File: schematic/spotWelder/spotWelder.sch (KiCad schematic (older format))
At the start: 18 parts, among them J1 InterBoard, Q1 Q_NPN_BCE, SW1 Rotary_Encoder_Switch, U1 STM32F103CBTx, U2 SSD1306-I2C-OLED-128x64, U3 DC/DC converter

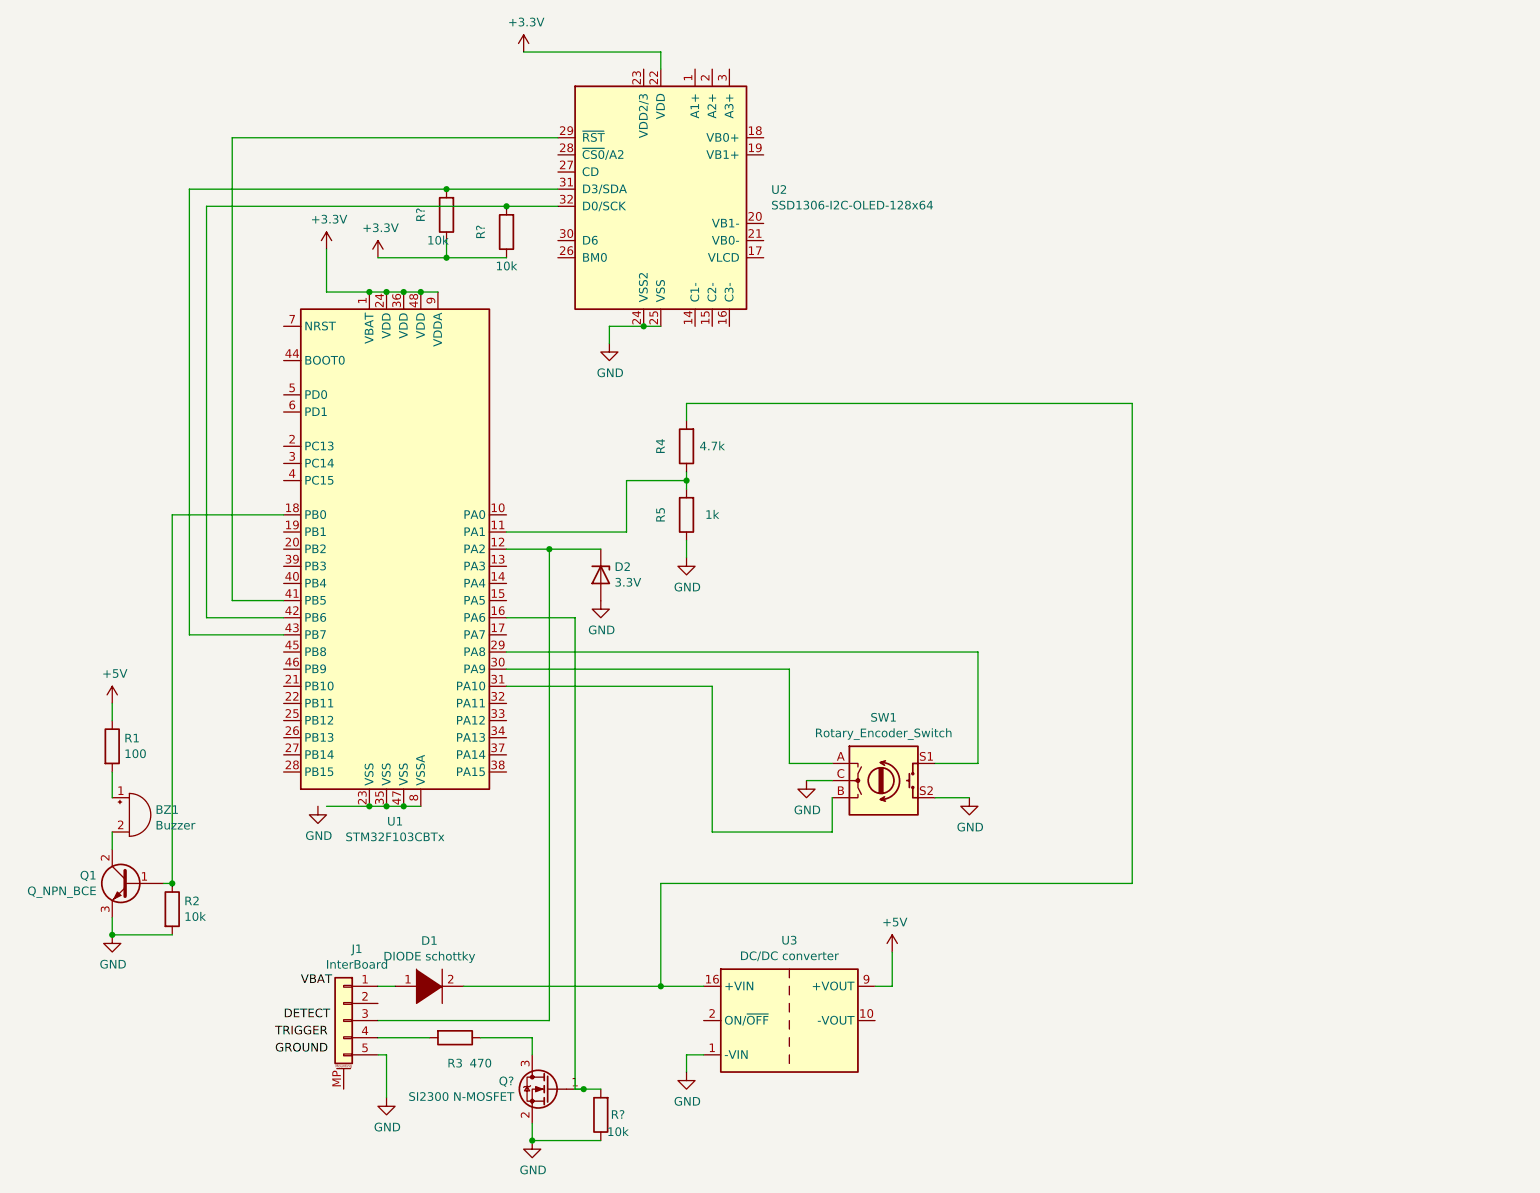
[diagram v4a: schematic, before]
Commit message: add pedal to schematic
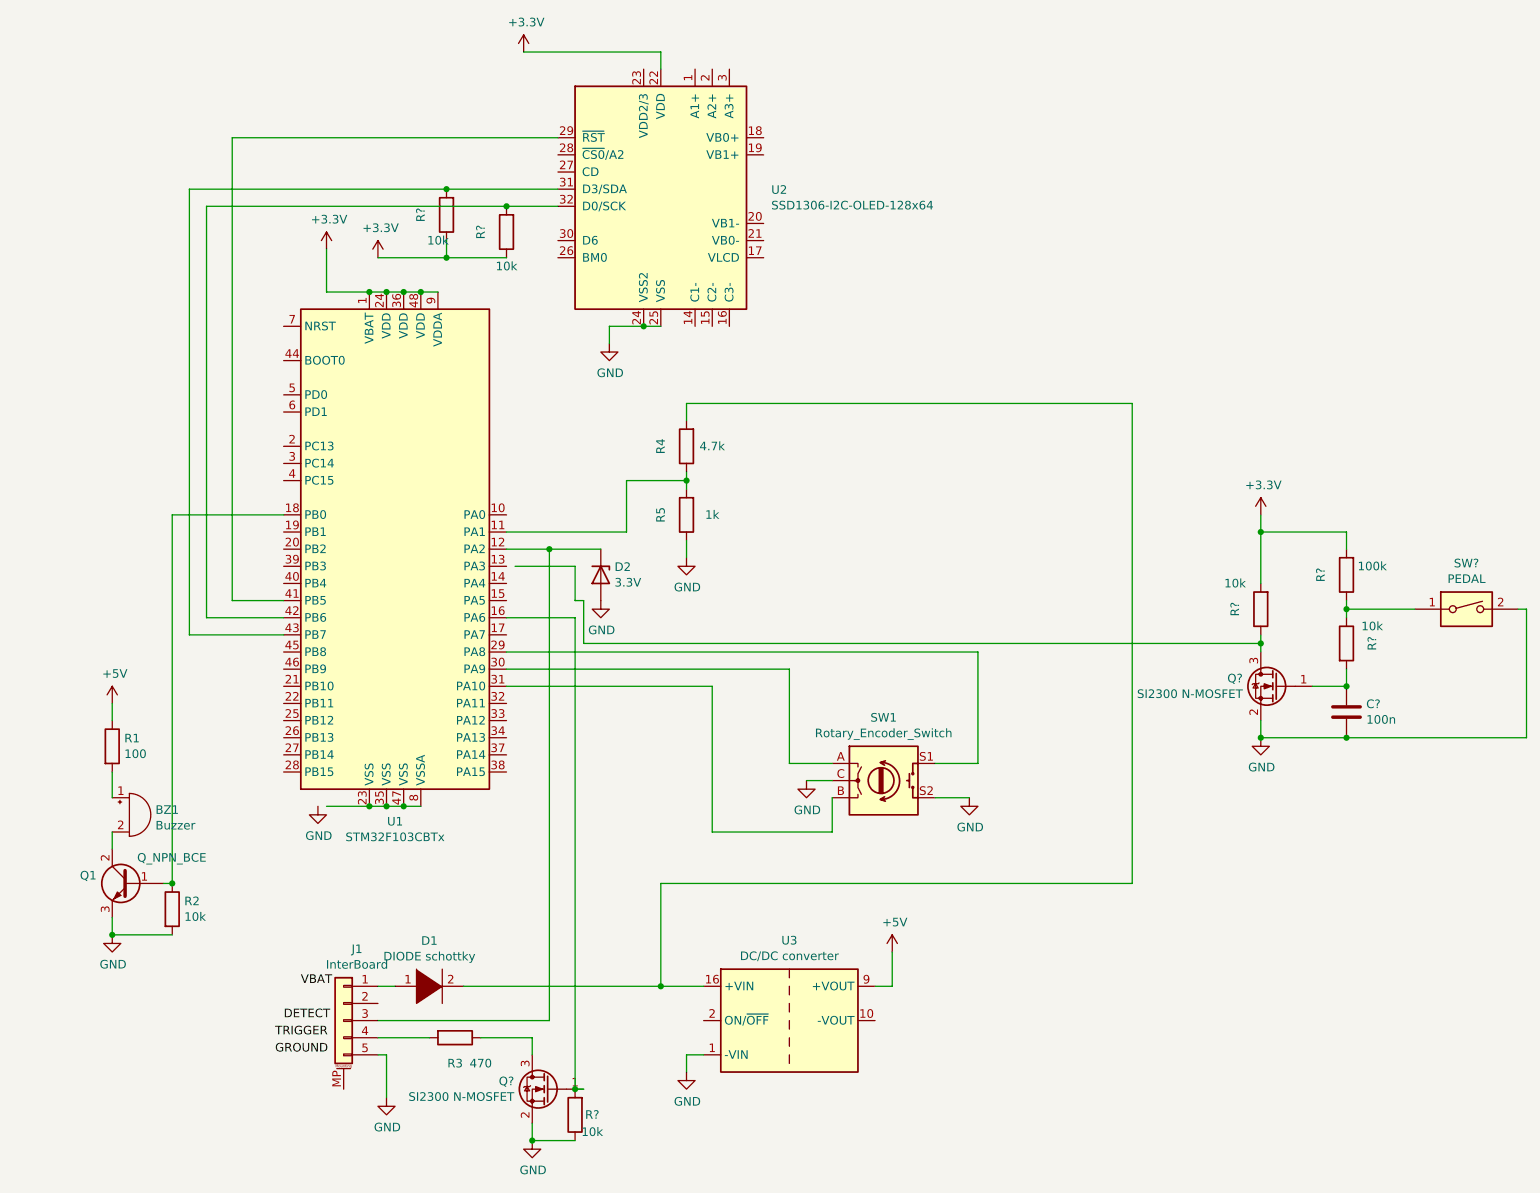
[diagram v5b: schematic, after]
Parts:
- added C?: 100n, symbol Device:C
- added Q?: SI2300 N-MOSFET, Package_TO_SOT_SMD:SOT-23, symbol Transistor_FET:ZXMN2A01F
- added R? (x2): 10k, symbol Device:R
- added R?: 100k, symbol Device:R
- added SW?: PEDAL, symbol Switch:SW_DIP_x01
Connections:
- net +3V3: now also R?.2, R?.2
- net GND: now also C?.2, Q?.2 (S), SW?.2
- new net: C?.1, Q?.1 (G), R?.2
- new net: Q?.3 (D), R?.1
- new net: R?.1, R?.1, SW?.1
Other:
- moved on the sheet: R?
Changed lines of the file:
@@
 P 900 5550
 F 0 "Q1" H 1091 5596 50  0000 L CNN
-F 1 "Q_NPN_BCE" H 1091 5505 50  0000 L CNN
+F 1 "Q_NPN_BCE" H 450 5700 50  0000 L CNN
 F 2 "" H 1100 5650 50  0001 C CNN
 F 3 "~" H 900 5550 50  0001 C CNN
@@
 L Device:R R?
 U 1 1 606079F6
-P 3650 6900
-F 0 "R?" H 3550 6900 50  0000 C CNN
-F 1 "10k" H 3550 7000 50  0000 C CNN
-F 2 "" V 3580 6900 50  0001 C CNN
-F 3 "~" H 3650 6900 50  0001 C CNN
-	1    3650 6900
-	-1   0    0    1
-$EndComp
-Wire Wire Line
-	3550 6750 3650 6750
-Wire Wire Line
-	3650 7050 3250 7050
+P 3500 6900
+F 0 "R?" H 3400 6900 50  0000 C CNN
+F 1 "10k" H 3400 7000 50  0000 C CNN
+F 2 "" V 3430 6900 50  0001 C CNN
+F 3 "~" H 3500 6900 50  0001 C CNN
+	1    3500 6900
+	-1   0    0    1
+$EndComp
 Connection ~ 3250 7050
 Wire Wire Line
 	3500 4000 3500 6750
-Wire Wire Line
-	3500 6750 3550 6750
-Connection ~ 3550 6750
+$Comp
+L Transistor_FET:ZXMN2A01F Q?
+U 1 1 6062FDB3
+P 7600 4400
+F 0 "Q?" H 7805 4446 50  0000 L CNN
+F 1 "SI2300 N-MOSFET" H 7805 4355 50  0000 L CNN
+F 2 "Package_TO_SOT_SMD:SOT-23" H 7800 4325 50  0001 L CIN
+F 3 "http://www.diodes.com/assets/Datasheets/ZXMN2A01F.pdf" H 7600 4400 50  0001 L CNN
+	1    7600 4400
+	-1   0    0    -1
+$EndComp
+$Comp
+L power:GND #PWR?
+U 1 1 606358E9
+P 7500 4700
+F 0 "#PWR?" H 7500 4450 50  0001 C CNN
+F 1 "GND" H 7505 4527 50  0000 C CNN
+F 2 "" H 7500 4700 50  0001 C CNN
+F 3 "" H 7500 4700 50  0001 C CNN
+	1    7500 4700
+	1    0    0    -1
+$EndComp
+$Comp
+L power:+3.3V #PWR?
+U 1 1 60637134
+P 7500 3400
+F 0 "#PWR?" H 7500 3250 50  0001 C CNN
+F 1 "+3.3V" H 7515 3573 50  0000 C CNN
+F 2 "" H 7500 3400 50  0001 C CNN
+F 3 "" H 7500 3400 50  0001 C CNN
+	1    7500 3400
+	1    0    0    -1
+$EndComp
+$Comp
+L Device:R R?
+U 1 1 60639461
+P 8000 4150
+F 0 "R?" V 8150 4150 50  0000 C CNN
+F 1 "10k" H 8150 4250 50  0000 C CNN
+F 2 "" V 7930 4150 50  0001 C CNN
+F 3 "~" H 8000 4150 50  0001 C CNN
+	1    8000 4150
+	1    0    0    -1
+$EndComp
+$Comp
+L Device:R R?
+U 1 1 6063CBA6
+P 8000 3750
+F 0 "R?" V 8150 3750 50  0000 C CNN
+F 1 "100k" H 7850 3700 50  0000 C CNN
+F 2 "" V 7930 3750 50  0001 C CNN
+F 3 "~" H 8000 3750 50  0001 C CNN
+	1    8000 3750
+	-1   0    0    1
+$EndComp
+$Comp
+L Device:R R?
+U 1 1 6063D28E
+P 7500 3950
+F 0 "R?" V 7650 3950 50  0000 C CNN
+F 1 "10k" H 7650 3800 50  0000 C CNN
+F 2 "" V 7430 3950 50  0001 C CNN
+F 3 "~" H 7500 3950 50  0001 C CNN
+	1    7500 3950
+	-1   0    0    1
+$EndComp
+Wire Wire Line
+	7500 4600 7500 4700
+Connection ~ 7500 4700
+Wire Wire Line
+	7500 4200 7500 4150
+Wire Wire Line
+	3150 3700 3500 3700
+Wire Wire Line
+	3500 3700 3500 3900
+Wire Wire Line
+	3500 3900 3550 3900
+Wire Wire Line
+	3550 3900 3550 4150
+Connection ~ 7500 4150
+Wire Wire Line
+	7500 4150 7500 4100
+$Comp
+L Device:C C?
+U 1 1 6065972F
+P 8000 4550
+F 0 "C?" H 8115 4596 50  0000 L CNN
+F 1 "100n" H 8115 4505 50  0000 L CNN
+F 2 "" H 8038 4400 50  0001 C CNN
+F 3 "~" H 8000 4550 50  0001 C CNN
+	1    8000 4550
+	1    0    0    -1
+$EndComp
+Wire Wire Line
+	7500 4700 8000 4700
+$Comp
+L Switch:SW_DIP_x01 SW?
+U 1 1 6066CEBA
+P 8700 3950
+F 0 "SW?" H 8700 4217 50  0000 C CNN
+F 1 "PEDAL" H 8700 4126 50  0000 C CNN
+F 2 "" H 8700 3950 50  0001 C CNN
+F 3 "~" H 8700 3950 50  0001 C CNN
+	1    8700 3950
+	1    0    0    -1
+$EndComp
+Wire Wire Line
+	7800 4400 8000 4400
+Connection ~ 8000 4700
+Wire Wire Line
+	8000 4700 9050 4700
+Wire Wire Line
+	7500 3400 7500 3500
+Wire Wire Line
+	7500 3500 8000 3500
+Wire Wire Line
+	8000 3500 8000 3600
+Connection ~ 7500 3500
+Wire Wire Line
+	7500 3500 7500 3800
+Wire Wire Line
+	8000 3900 8000 3950
+Wire Wire Line
+	8000 4300 8000 4400
+Connection ~ 8000 4400
+Wire Wire Line
+	9000 3950 9050 3950
+Wire Wire Line
+	9050 3950 9050 4700
+Wire Wire Line
+	8400 3950 8000 3950
+Connection ~ 8000 3950
+Wire Wire Line
+	8000 3950 8000 4000
+Wire Wire Line
+	3500 7050 3250 7050
+Wire Wire Line
+	3550 6750 3500 6750
+Connection ~ 3500 6750
+Wire Wire Line
+	3550 4150 7500 4150
 $EndSCHEMATC

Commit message: update schematic
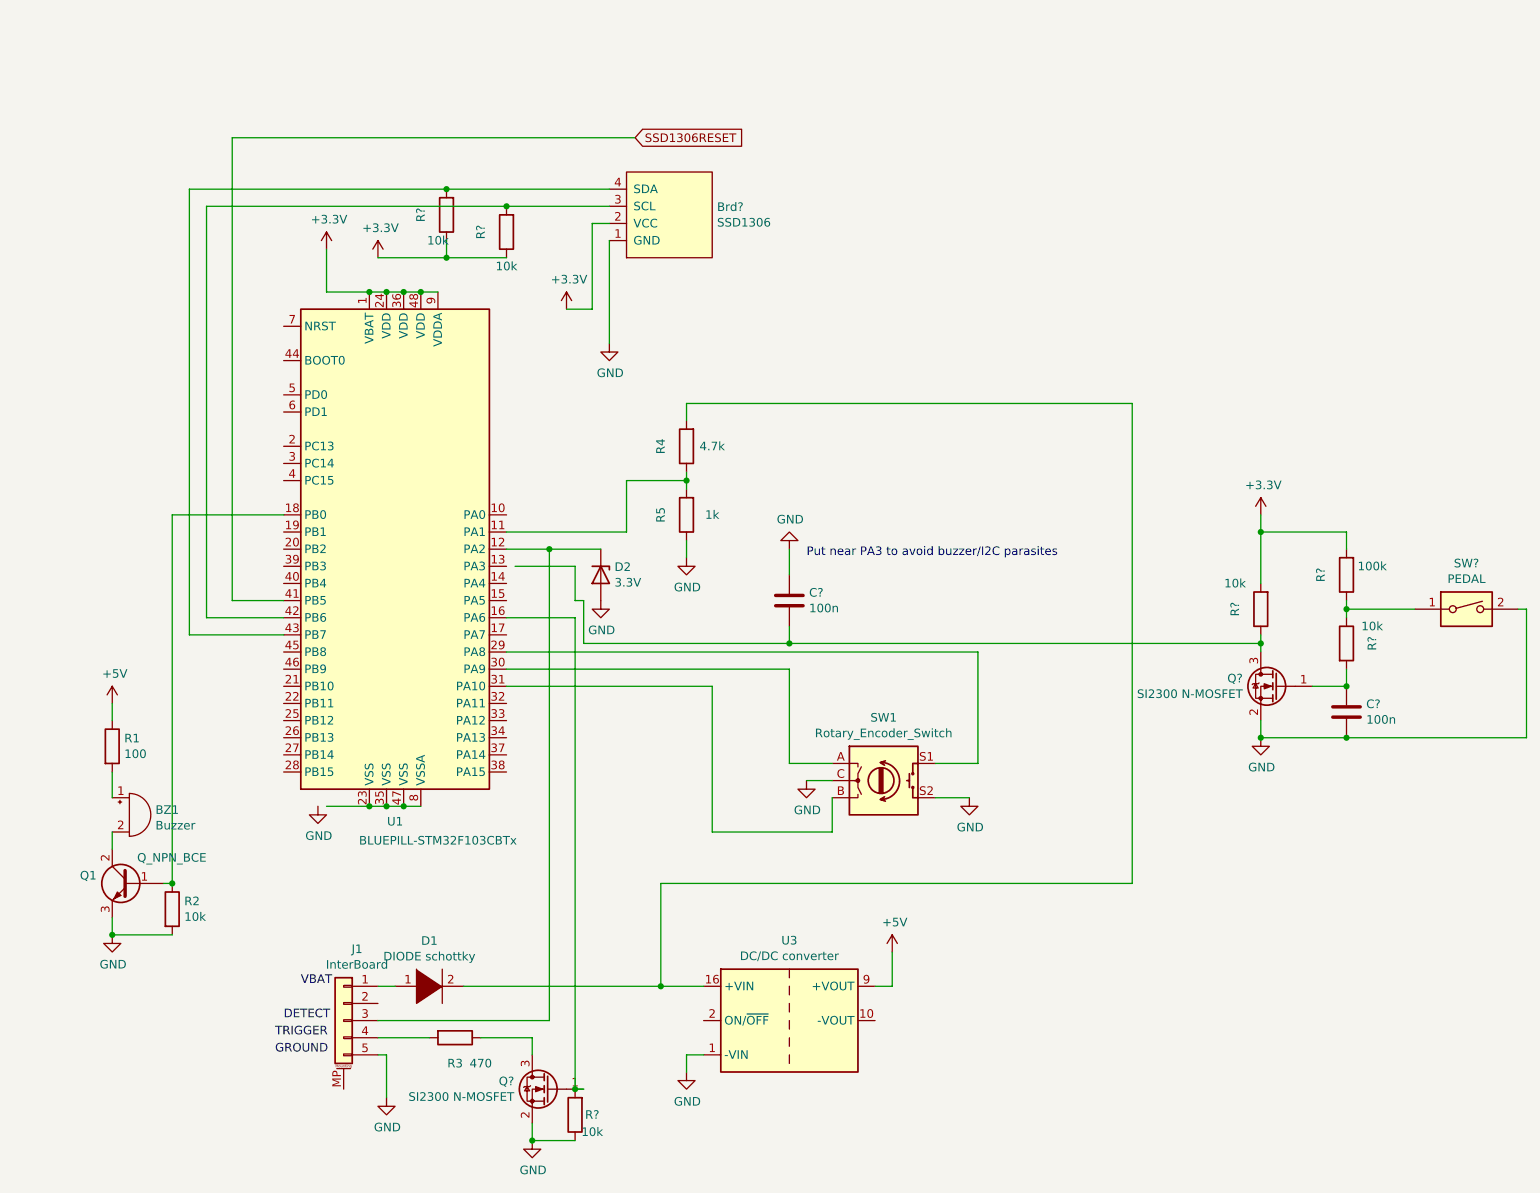
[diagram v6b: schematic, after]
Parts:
- removed U2: SSD1306-I2C-OLED-128x64, Display:EA_DOGXL160-7, symbol Display_Graphic:EA_DOGXL160-7
- added Brd?: SSD1306, symbol SSD1306-128x64_OLED:SSD1306
- added C?: 100n, symbol Device:C
- U1: value STM32F103CBTx -> BLUEPILL-STM32F103CBTx
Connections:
- net +3V3: now also Brd?.2 (VCC)
- net GND: now also Brd?.1 (GND), C?.1
- net SSD1306RESET: now reaches U1.41 (PB5)
- net at R?.2, U1.42 (PB6): now also Brd?.3 (SCL)
- net at R?.2, U1.43 (PB7): now also Brd?.4 (SDA)
- net at Q?.3 (D), R?.1: now also C?.2
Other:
- note added: "Put near PA3 to avoid buzzer/I2C parasites"
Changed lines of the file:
@@
 P 2500 3600
 F 0 "U1" H 2450 2011 50  0000 C CNN
-F 1 "STM32F103CBTx" H 2450 1920 50  0000 C CNN
+F 1 "BLUEPILL-STM32F103CBTx" H 2700 1900 50  0000 C CNN
 F 2 "Package_QFP:LQFP-48_7x7mm_P0.5mm" H 1900 2200 50  0001 R CNN
 F 3 "http://www.st.com/st-web-ui/static/active/en/resource/technical/document/datasheet/CD00161566.pdf" H 2500 3600 50  0001 C CNN
@@
 	1    0    0    -1
 $EndComp
-$Comp
-L Display_Graphic:EA_DOGXL160-7 U2
-U 1 1 6058DB7E
-P 4000 1500
-F 0 "U2" H 4644 1496 50  0000 L CNN
-F 1 "SSD1306-I2C-OLED-128x64" H 4644 1405 50  0000 L CNN
-F 2 "Display:EA_DOGXL160-7" H 4000 500 50  0001 C CNN
-F 3 "http://www.lcd-module.com/eng/pdf/grafik/dogxl160-7e.pdf" H 1650 2650 50  0001 C CNN
-	1    4000 1500
-	1    0    0    -1
-$EndComp
 Wire Wire Line
 	1500 3900 1800 3900
@@
 	1    0    0    -1
 $EndComp
-Wire Wire Line
-	3700 2300 3700 2400
 $Comp
 L power:+3.3V #PWR06
 U 1 1 605967BF
-P 3200 700
-F 0 "#PWR06" H 3200 550 50  0001 C CNN
-F 1 "+3.3V" H 3215 873 50  0000 C CNN
-F 2 "" H 3200 700 50  0001 C CNN
-F 3 "" H 3200 700 50  0001 C CNN
-	1    3200 700
+P 3450 2200
+F 0 "#PWR06" H 3450 2050 50  0001 C CNN
+F 1 "+3.3V" H 3465 2373 50  0000 C CNN
+F 2 "" H 3450 2200 50  0001 C CNN
+F 3 "" H 3450 2200 50  0001 C CNN
+	1    3450 2200
 	1    0    0    -1
 $EndComp
@@
 	5350 5950 5350 6150
 Wire Wire Line
-	3700 2300 3900 2300
-Connection ~ 3900 2300
-Wire Wire Line
-	3900 2300 4000 2300
-Wire Wire Line
-	4000 800  4000 700
-Wire Wire Line
-	4000 700  3200 700
-Wire Wire Line
 	1500 3900 1500 1200
 Wire Wire Line
-	1500 1200 3400 1200
-Wire Wire Line
-	3400 1600 3100 1600
-Wire Wire Line
 	1350 1600 1350 4000
 Wire Wire Line
 	1350 4000 1800 4000
-Wire Wire Line
-	3400 1500 2750 1500
 Wire Wire Line
 	1250 1500 1250 4100
@@
 Connection ~ 3500 6750
 Wire Wire Line
-	3550 4150 7500 4150
+	3550 4150 4750 4150
+$Comp
+L Device:C C?
+U 1 1 6068B873
+P 4750 3900
+F 0 "C?" H 4865 3946 50  0000 L CNN
+F 1 "100n" H 4865 3855 50  0000 L CNN
+F 2 "" H 4788 3750 50  0001 C CNN
+F 3 "~" H 4750 3900 50  0001 C CNN
+	1    4750 3900
+	1    0    0    -1
+$EndComp
+$Comp
+L power:GND #PWR?
+U 1 1 6068C6CA
+P 4750 3600
+F 0 "#PWR?" H 4750 3350 50  0001 C CNN
+F 1 "GND" H 4755 3427 50  0000 C CNN
+F 2 "" H 4750 3600 50  0001 C CNN
+F 3 "" H 4750 3600 50  0001 C CNN
+	1    4750 3600
+	1    0    0    1
+$EndComp
+Wire Wire Line
+	4750 3600 4750 3750
+Wire Wire Line
+	4750 4050 4750 4150
+Connection ~ 4750 4150
+Wire Wire Line
+	4750 4150 7500 4150
+Text Notes 4850 3650 0    50   ~ 0
+Put near PA3 to avoid buzzer/I2C parasites
+$Comp
+L SSD1306-128x64_OLED:SSD1306 Brd?
+U 1 1 606A4189
+P 4050 1650
+F 0 "Brd?" V 4096 1372 50  0000 R CNN
+F 1 "SSD1306" V 4005 1372 50  0000 R CNN
+F 2 "" H 4050 1900 50  0001 C CNN
+F 3 "" H 4050 1900 50  0001 C CNN
+	1    4050 1650
+	0    -1   -1   0
+$EndComp
+Wire Wire Line
+	3450 2200 3600 2200
+Wire Wire Line
+	3600 2200 3600 1700
+Wire Wire Line
+	3600 1700 3700 1700
+Wire Wire Line
+	3700 1800 3700 2400
+Wire Wire Line
+	2750 1500 3700 1500
+Wire Wire Line
+	3100 1600 3700 1600
+Text GLabel 3850 1200 2    50   Input ~ 0
+SSD1306RESET
+Wire Wire Line
+	1500 1200 3850 1200
 $EndSCHEMATC

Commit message: add WS2812B
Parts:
- added D? (x3): WS2812B, LED_SMD:LED_WS2812B_PLCC4_5.0x5.0mm_P3.2mm, symbol LED:WS2812B
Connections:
- net +5V: now also D?.1 (VDD), D?.1 (VDD), D?.1 (VDD)
- net GND: now also D?.3 (VSS), D?.3 (VSS)
- net at U1.17 (PA7): now also D?.4 (DIN)
- new net: D?.2 (DOUT), D?.4 (DIN) (x2)
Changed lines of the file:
@@
 Wire Wire Line
 	1500 1200 3850 1200
+$Comp
+L LED:WS2812B D?
+U 1 1 60715C50
+P 5600 1450
+F 0 "D?" H 5944 1496 50  0000 L CNN
+F 1 "WS2812B" H 5944 1405 50  0000 L CNN
+F 2 "LED_SMD:LED_WS2812B_PLCC4_5.0x5.0mm_P3.2mm" H 5650 1150 50  0001 L TNN
+F 3 "https://cdn-shop.adafruit.com/datasheets/WS2812B.pdf" H 5700 1075 50  0001 L TNN
+	1    5600 1450
+	1    0    0    -1
+$EndComp
+$Comp
+L LED:WS2812B D?
+U 1 1 6071688E
+P 6500 1450
+F 0 "D?" H 6844 1496 50  0000 L CNN
+F 1 "WS2812B" H 6844 1405 50  0000 L CNN
+F 2 "LED_SMD:LED_WS2812B_PLCC4_5.0x5.0mm_P3.2mm" H 6550 1150 50  0001 L TNN
+F 3 "https://cdn-shop.adafruit.com/datasheets/WS2812B.pdf" H 6600 1075 50  0001 L TNN
+	1    6500 1450
+	1    0    0    -1
+$EndComp
+$Comp
+L LED:WS2812B D?
+U 1 1 6071772C
+P 7400 1450
+F 0 "D?" H 7744 1496 50  0000 L CNN
+F 1 "WS2812B" H 7744 1405 50  0000 L CNN
+F 2 "LED_SMD:LED_WS2812B_PLCC4_5.0x5.0mm_P3.2mm" H 7450 1150 50  0001 L TNN
+F 3 "https://cdn-shop.adafruit.com/datasheets/WS2812B.pdf" H 7500 1075 50  0001 L TNN
+	1    7400 1450
+	1    0    0    -1
+$EndComp
+$Comp
+L power:+5V #PWR?
+U 1 1 60718FBB
+P 6500 950
+F 0 "#PWR?" H 6500 800 50  0001 C CNN
+F 1 "+5V" H 6515 1123 50  0000 C CNN
+F 2 "" H 6500 950 50  0001 C CNN
+F 3 "" H 6500 950 50  0001 C CNN
+	1    6500 950
+	1    0    0    -1
+$EndComp
+$Comp
+L power:GND #PWR?
+U 1 1 60719C76
+P 6500 1950
+F 0 "#PWR?" H 6500 1700 50  0001 C CNN
+F 1 "GND" H 6505 1777 50  0000 C CNN
+F 2 "" H 6500 1950 50  0001 C CNN
+F 3 "" H 6500 1950 50  0001 C CNN
+	1    6500 1950
+	1    0    0    -1
+$EndComp
+Wire Wire Line
+	5600 1150 6500 1150
+Wire Wire Line
+	5600 1750 6500 1750
+Wire Wire Line
+	6500 1750 6500 1950
+Connection ~ 6500 1750
+Wire Wire Line
+	6500 1150 6500 950
+Connection ~ 6500 1150
+Wire Wire Line
+	6500 1150 7400 1150
+Wire Wire Line
+	7350 1750 6500 1750
+Wire Wire Line
+	5900 1450 6200 1450
+Wire Wire Line
+	6800 1450 7100 1450
+Wire Wire Line
+	3100 4100 3300 4100
+Wire Wire Line
+	3300 4100 3300 2950
+Wire Wire Line
+	3300 2950 3950 2950
+Wire Wire Line
+	3950 2950 3950 2400
+Wire Wire Line
+	3950 2400 4900 2400
+Wire Wire Line
+	4900 2400 4900 1450
+Wire Wire Line
+	4900 1450 5300 1450
 $EndSCHEMATC

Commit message: update README
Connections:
- net at U1.13 (PA3): now also C?.2, Q?.3 (D), R?.1
- net at Q?.1 (G), R?.2: now also U1.19 (PB1); no longer U1.16 (PA6)
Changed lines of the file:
@@
 	2350 6450 2650 6450
-Wire Wire Line
-	3100 4000 3500 4000
 Wire Wire Line
 	2350 6350 3350 6350
@@
 $EndComp
 Connection ~ 3250 7050
-Wire Wire Line
-	3500 4000 3500 6750
 $Comp
 L Transistor_FET:ZXMN2A01F Q?
@@
 	7500 4200 7500 4150
 Wire Wire Line
-	3150 3700 3500 3700
-Wire Wire Line
 	3500 3700 3500 3900
 Wire Wire Line
@@
 Wire Wire Line
 	3550 6750 3500 6750
-Connection ~ 3500 6750
 Wire Wire Line
 	3550 4150 4750 4150
@@
 Wire Wire Line
 	4900 1450 5300 1450
+Wire Wire Line
+	3100 3700 3500 3700
+Wire Wire Line
+	1800 3500 1650 3500
+Wire Wire Line
+	1650 3500 1650 5600
+Wire Wire Line
+	1650 5600 3500 5600
+Wire Wire Line
+	3500 5600 3500 6750
+Connection ~ 3500 6750
 $EndSCHEMATC
